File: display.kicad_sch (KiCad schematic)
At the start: 26 parts, among them J701 Socket_Molex_SlimStack_2x20_5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, J702 HDMI-A_WE_685119134923

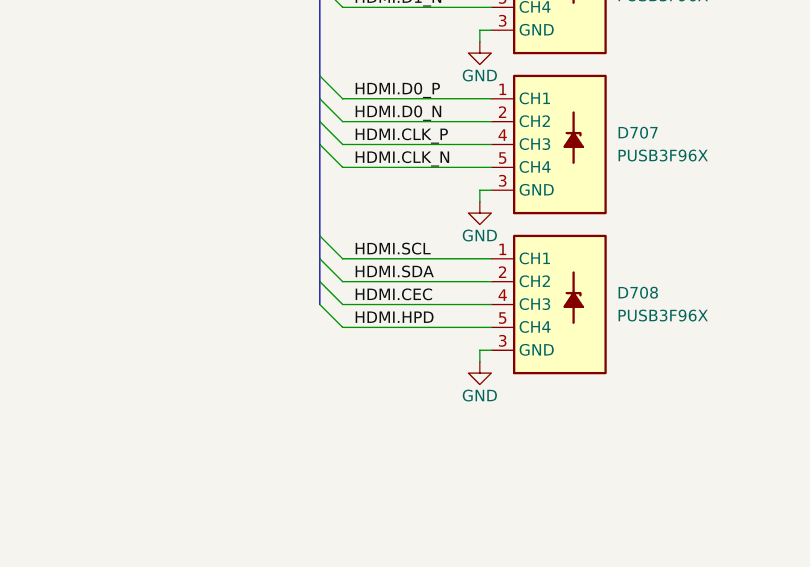
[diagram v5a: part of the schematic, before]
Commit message: [#55532] PCB: HDMI & DSI adapter conns related routing
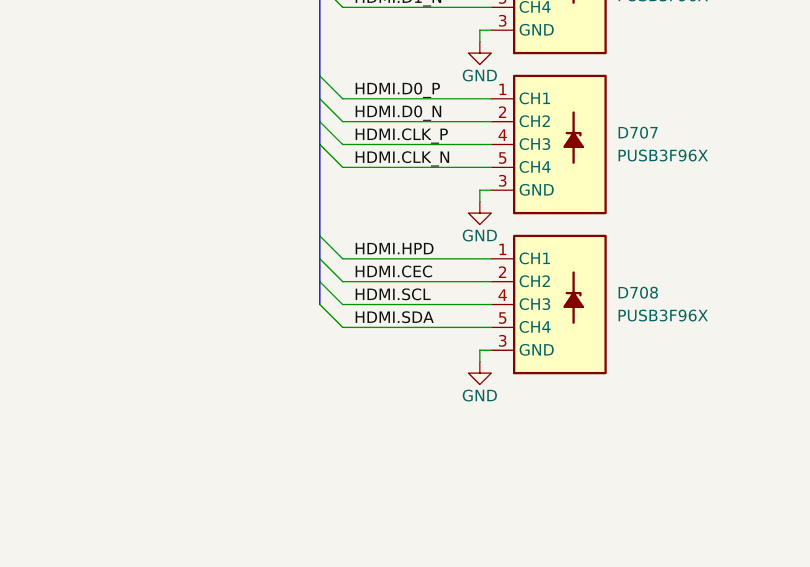
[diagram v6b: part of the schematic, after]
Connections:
- net HDMI.CEC: now also D708.2 (CH2), D708.9 (CH2); no longer D708.4 (CH3), D708.7 (CH3)
- net HDMI.HPD: now also D708.1 (CH1), D708.10 (CH1); no longer D708.5 (CH4), D708.6 (CH4)
- net HDMI.SCL: now also D708.4 (CH3), D708.7 (CH3); no longer D708.1 (CH1), D708.10 (CH1)
- net HDMI.SDA: now also D708.5 (CH4), D708.6 (CH4); no longer D708.2 (CH2), D708.9 (CH2)
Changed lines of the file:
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@@
     (effects (font (size 1.27 1.27)) (justify left bottom))
   )
-  (label "HDMI.HPD" (at 162.56 83.82 0) (fields_autoplaced)
+  (label "HDMI.HPD" (at 162.56 76.2 0) (fields_autoplaced)
     (effects (font (size 1.27 1.27)) (justify left bottom))
   )
-  (label "HDMI.SDA" (at 162.56 78.74 0) (fields_autoplaced)
+  (label "HDMI.SDA" (at 162.56 83.82 0) (fields_autoplaced)
     (effects (font (size 1.27 1.27)) (justify left bottom))
   )
@@
     (effects (font (size 1.27 1.27)) (justify left bottom))
   )
-  (label "HDMI.SCL" (at 162.56 76.2 0) (fields_autoplaced)
+  (label "HDMI.SCL" (at 162.56 81.28 0) (fields_autoplaced)
     (effects (font (size 1.27 1.27)) (justify left bottom))
   )
@@
     (effects (font (size 1.27 1.27)) (justify left bottom))
   )
-  (label "HDMI.CEC" (at 162.56 81.28 0) (fields_autoplaced)
+  (label "HDMI.CEC" (at 162.56 78.74 0) (fields_autoplaced)
     (effects (font (size 1.27 1.27)) (justify left bottom))
   )
